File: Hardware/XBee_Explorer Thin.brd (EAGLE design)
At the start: 45.7 x 54.6 mm, 129 parts, among them J4 QWIIC_RIGHT_ANGLE, Q2 3.1A/30V/105mΩ, U1 FSUSB30MUX_MSOP10, U2 AP63203, U3 ESD Diode, U5 ESD Diode, U6 CP210X

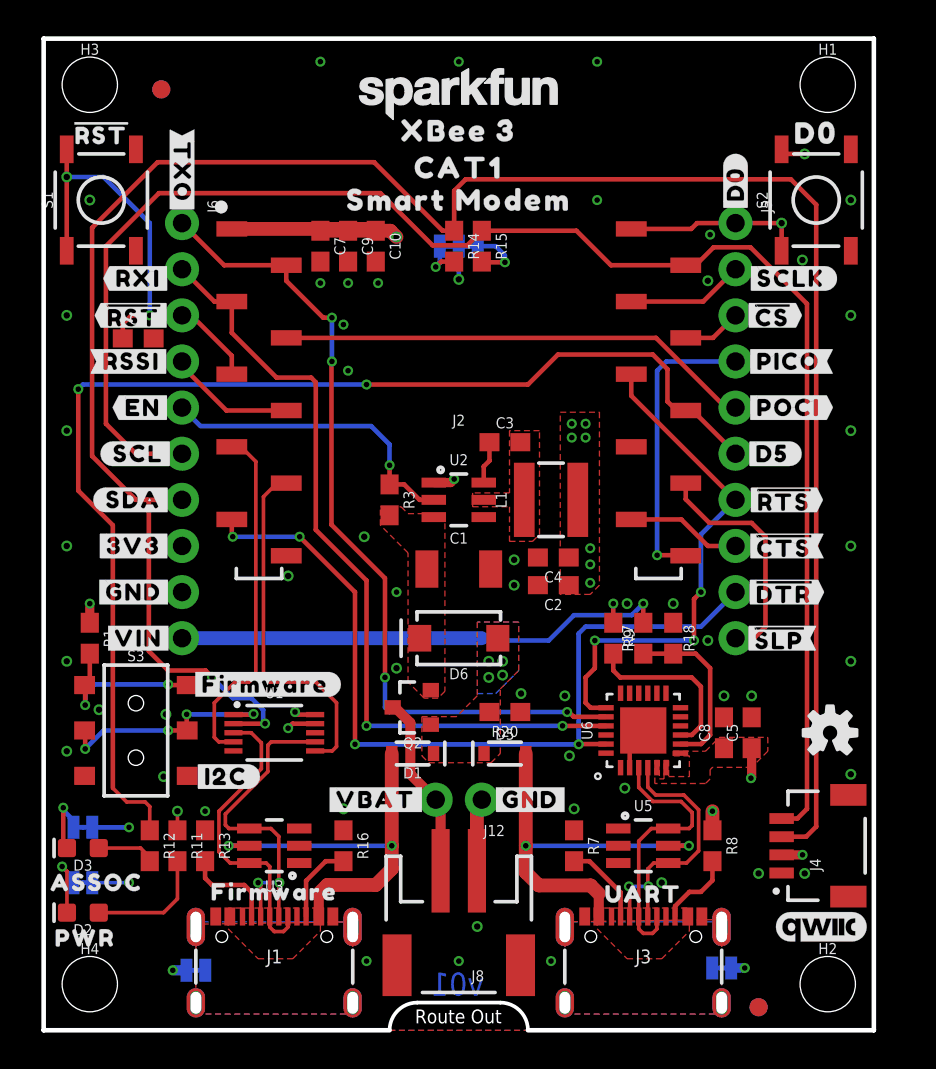
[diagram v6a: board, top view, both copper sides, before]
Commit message: Moves resistor colliding with switch, adds via under UART to serial IC, adds "1,2,3,4" in their respective layer
* Moves design to origin
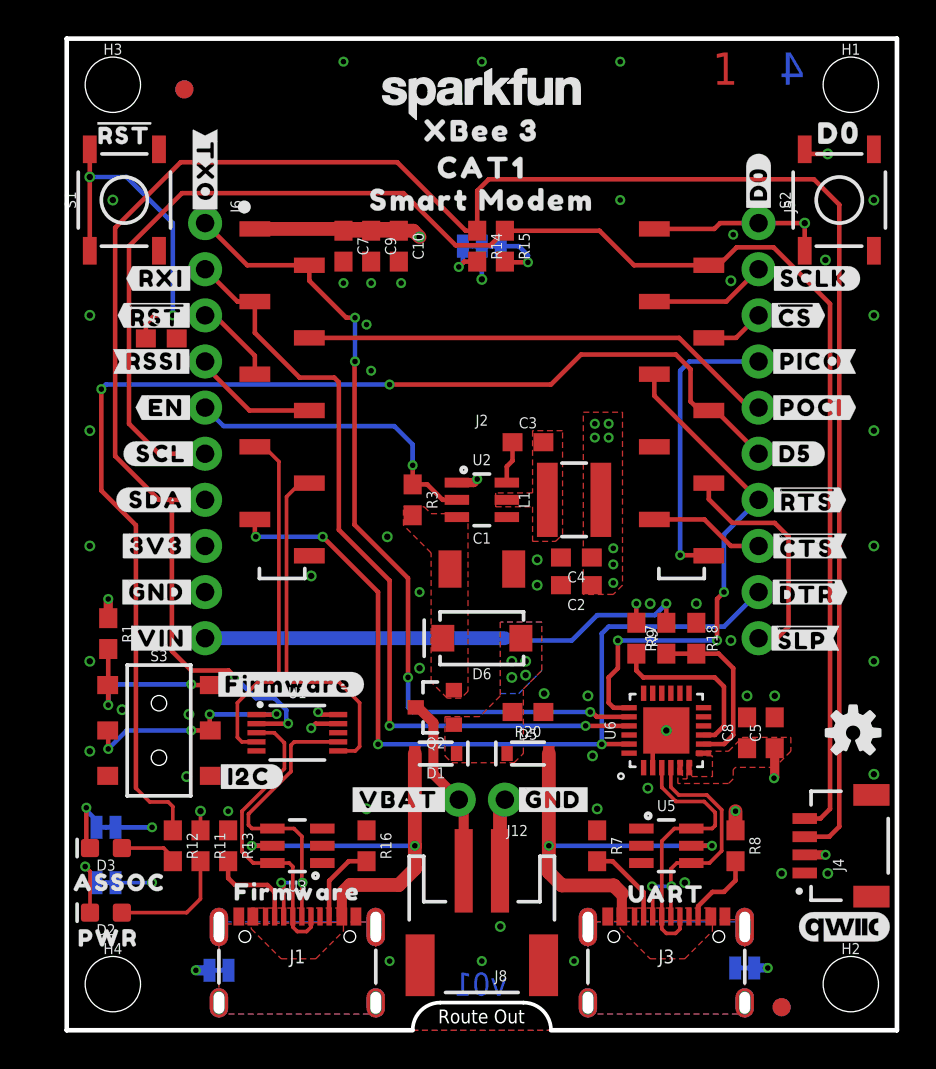
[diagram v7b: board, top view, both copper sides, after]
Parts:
- moved C8 1.27 mm to (37.5, 16.4)
- moved H1 1.27 mm to (43.2, 52.1)
- moved H2 1.27 mm to (43.2, 2.54)
- moved J3 1.27 mm to (33.0, 6.60)
- moved J4 1.27 mm to (40.6, 10.2)
- moved J5 1.27 mm to (38.1, 44.5)
- moved LOGO2 1.27 mm to (43.3, 16.4)
- moved R14 1.27 mm to (22.6, 43.2)
- moved R17 1.27 mm to (33.0, 21.6)
- moved S2 1.27 mm to (42.5, 45.7)
- moved SHLD 1.27 mm to (37.3, 3.43)
- moved U$10 1.27 mm to (38.1, 46.6)
- moved U$14 1.27 mm to (33.4, 34.3)
- moved U$28 1.27 mm to (41.0, 36.8)
- moved U$29 1.27 mm to (41.0, 34.3)
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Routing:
- net GND: vias 58 -> 59
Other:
- board text added: "1"
- board text added: "2"
- board text added: "3"
- board text added: "4"
